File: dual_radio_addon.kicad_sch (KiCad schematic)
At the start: 36 parts, among them J1 Mainboard, J2 Antenna switcher, J3 I2C, J4 I3C, U1 Module 1, U2 74LVC1GU04, U3 24C02BN, U4 Module 2, U5 74LVC1GU04, U6 Module 3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

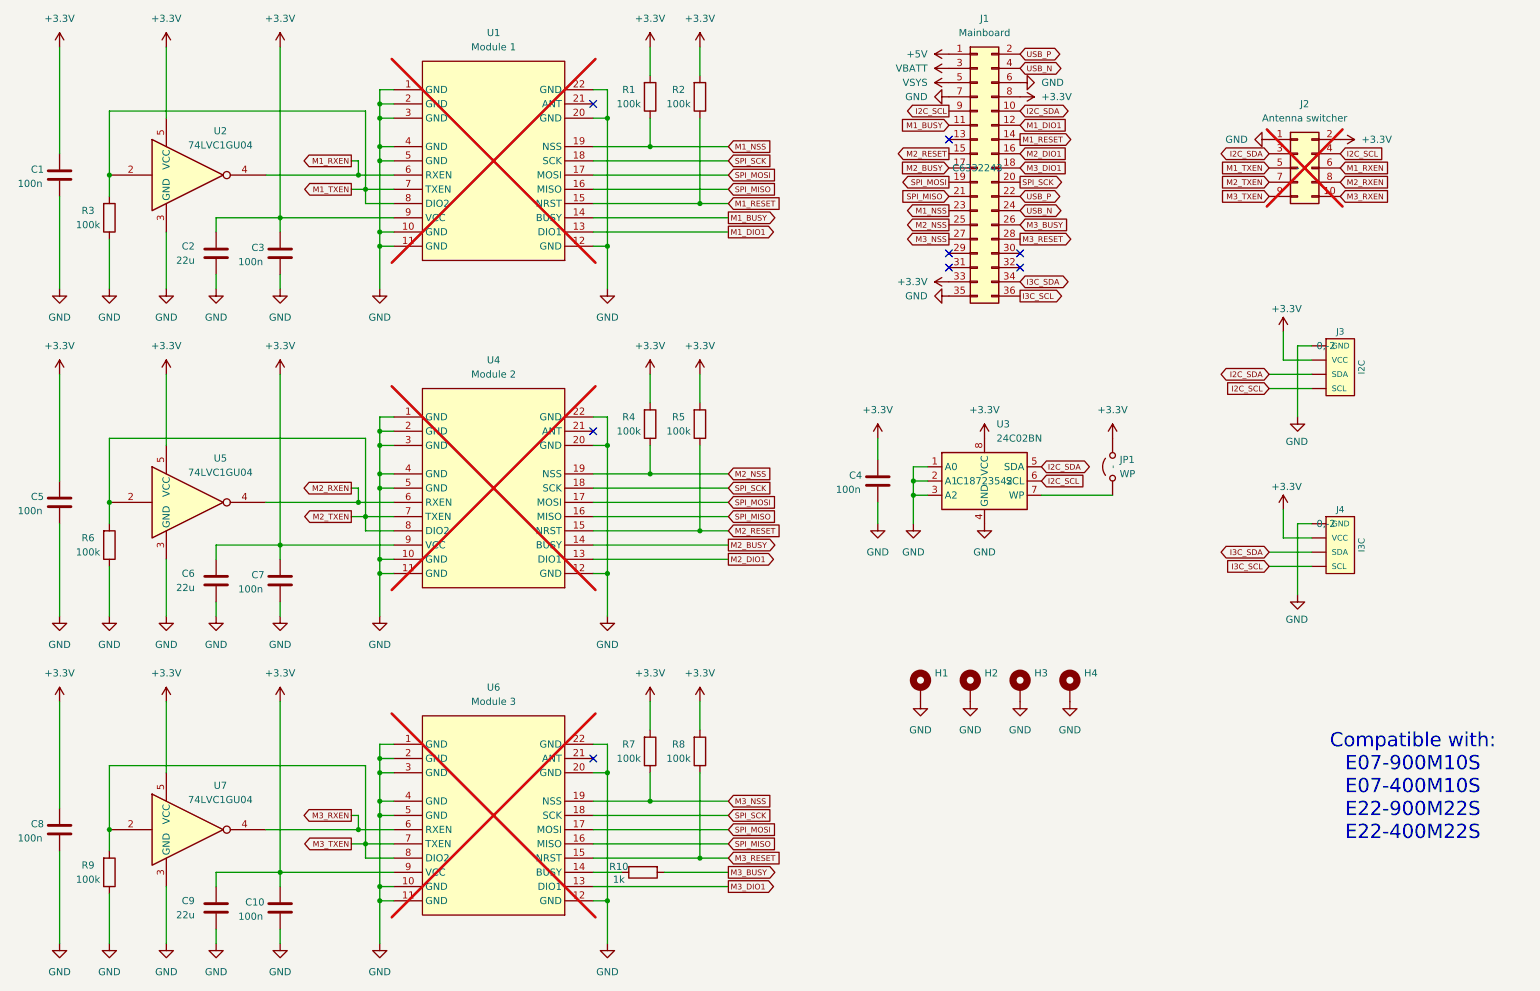
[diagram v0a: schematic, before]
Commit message: Fix connector orientation
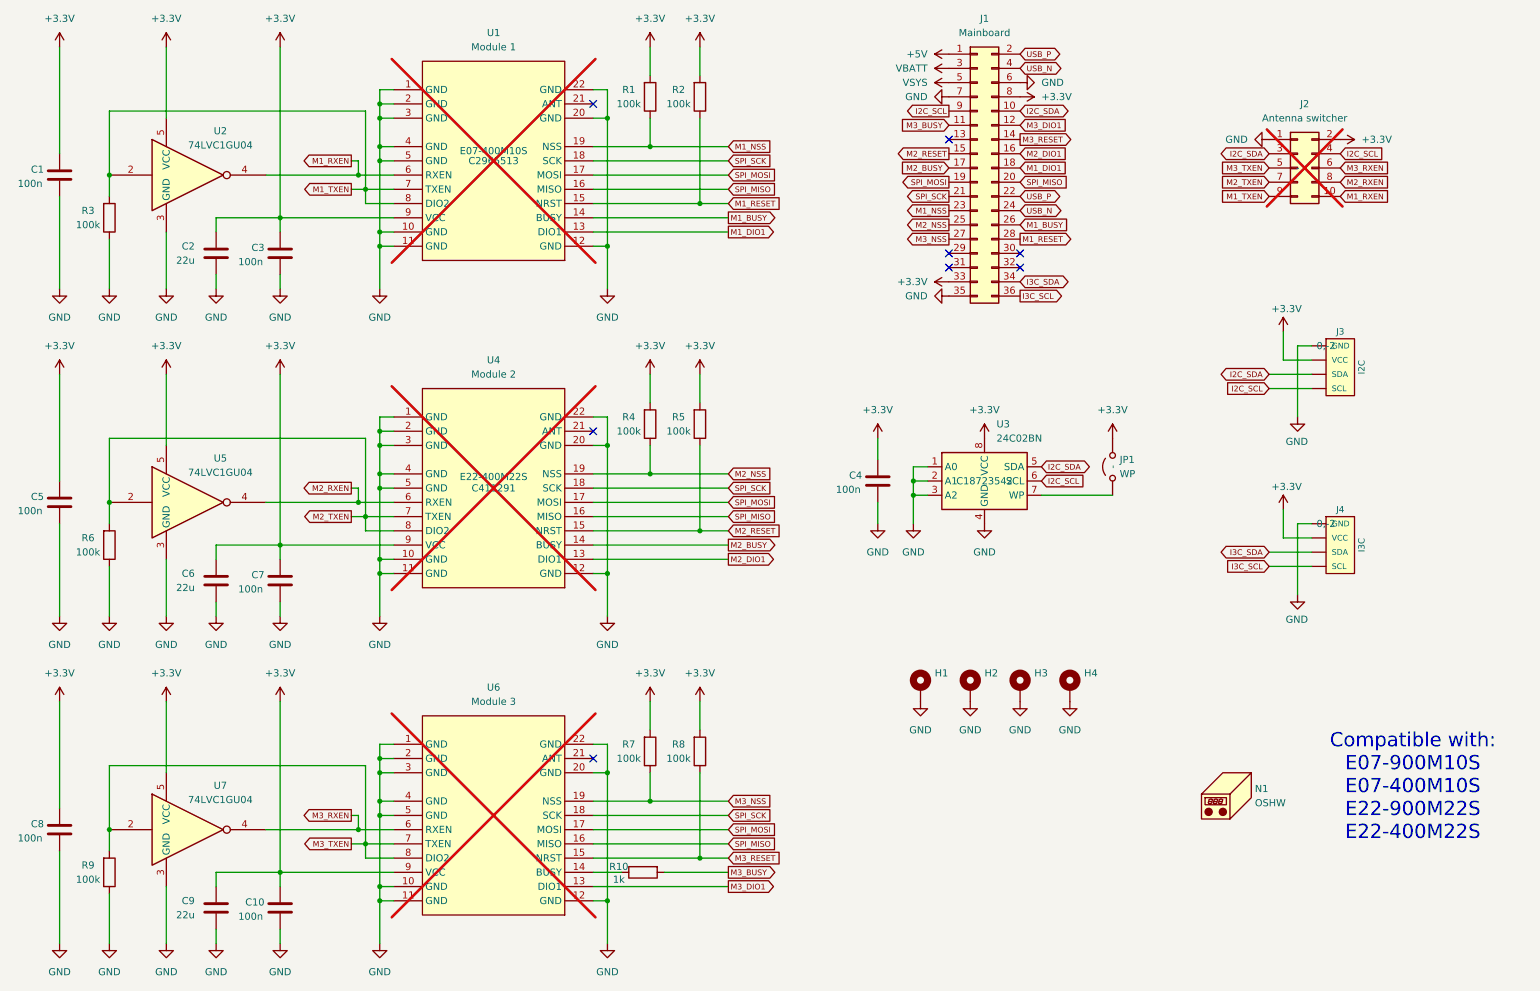
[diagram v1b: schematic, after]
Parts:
- added N1: OSHW, Symbol:OSHW-Logo2_9.8x8mm_SilkScreen, symbol Mechanical:Housing
- J2: footprint Connector_PinHeader_2.54mm:PinHeader_2x05_P2.54mm_Vertical_SMD -> Connector_PinHeader_2.54mm:PinHeader_2x05_P2.54mm_Vertical
- U1: LCSC - -> C2965513
- U4: LCSC - -> C411291
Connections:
- net M1_BUSY: now also J1.26 (Pin_26); no longer J1.11 (Pin_11)
- net M1_DIO1: now also J1.18 (Pin_18); no longer J1.12 (Pin_12)
- net M1_RESET: now also J1.28 (Pin_28); no longer J1.14 (Pin_14)
- net M1_RXEN: now also J2.10 (Pin_10); no longer J2.6 (Pin_6)
- net M1_TXEN: now also J2.9 (Pin_9); no longer J2.5 (Pin_5)
- net M3_BUSY: now also J1.11 (Pin_11); no longer J1.26 (Pin_26)
- net M3_DIO1: now also J1.12 (Pin_12); no longer J1.18 (Pin_18)
- net M3_RESET: now also J1.14 (Pin_14); no longer J1.28 (Pin_28)
- net M3_RXEN: now also J2.6 (Pin_6); no longer J2.10 (Pin_10)
- net M3_TXEN: now also J2.5 (Pin_5); no longer J2.9 (Pin_9)
- net SPI_MISO: now also J1.20 (Pin_20); no longer J1.21 (Pin_21)
- net SPI_SCK: now also J1.21 (Pin_21); no longer J1.20 (Pin_20)
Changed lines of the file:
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@@
 	(global_label "M1_DIO1"
 		(shape input)
-		(at 198.12 36.83 0)
+		(at 198.12 44.45 0)
 		(fields_autoplaced yes)
 		(effects
@@
 		)
 		(property "Intersheetrefs" "${INTERSHEET_REFS}"
-			(at 206.9425 36.83 0)
+			(at 206.9425 44.45 0)
 			(effects
 				(font
@@
 	(global_label "SPI_MISO"
 		(shape input)
-		(at 185.42 49.53 180)
+		(at 198.12 46.99 0)
 		(fields_autoplaced yes)
 		(effects
@@
 				(size 1.016 1.016)
 			)
-			(justify right)
+			(justify left)
 		)
 		(property "Intersheetrefs" "${INTERSHEET_REFS}"
-			(at 176.1137 49.53 0)
+			(at 207.4263 46.99 0)
 			(effects
 				(font
 					(size 1.27 1.27)
 				)
-				(justify right)
+				(justify left)
 				(hide yes)
 			)
@@
 	(global_label "M3_TXEN"
 		(shape input)
-		(at 242.57 49.53 180)
+		(at 242.57 44.45 180)
 		(fields_autoplaced yes)
 		(effects
@@
 		)
 		(property "Intersheetrefs" "${INTERSHEET_REFS}"
-			(at 233.554 49.53 0)
+			(at 233.554 44.45 0)
 			(effects
 				(font
@@
 	(global_label "M1_RESET"
 		(shape output)
-		(at 198.12 39.37 0)
+		(at 198.12 57.15 0)
 		(fields_autoplaced yes)
 		(effects
@@
 		)
 		(property "Intersheetrefs" "${INTERSHEET_REFS}"
-			(at 208.0068 39.37 0)
+			(at 208.0068 57.15 0)
 			(effects
 				(font
@@
 	(global_label "M1_RXEN"
 		(shape input)
-		(at 255.27 44.45 0)
+		(at 255.27 49.53 0)
 		(fields_autoplaced yes)
 		(effects
@@
 		)
 		(property "Intersheetrefs" "${INTERSHEET_REFS}"
-			(at 264.5279 44.45 0)
+			(at 264.5279 49.53 0)
 			(effects
 				(font
@@
 	(global_label "M3_DIO1"
 		(shape input)
-		(at 198.12 44.45 0)
+		(at 198.12 36.83 0)
 		(fields_autoplaced yes)
 		(effects
@@
 		)
 		(property "Intersheetrefs" "${INTERSHEET_REFS}"
-			(at 206.9425 44.45 0)
+			(at 206.9425 36.83 0)
 			(effects
 				(font
@@
 	(global_label "M3_BUSY"
 		(shape input)
-		(at 198.12 54.61 0)
+		(at 185.42 36.83 180)
 		(fields_autoplaced yes)
 		(effects
@@
 				(size 1.016 1.016)
 			)
-			(justify left)
+			(justify right)
 		)
 		(property "Intersheetrefs" "${INTERSHEET_REFS}"
-			(at 207.3296 54.61 0)
+			(at 176.2104 36.83 0)
 			(effects
 				(font
 					(size 1.27 1.27)
 				)
-				(justify left)
+				(justify right)
 				(hide yes)
 			)
@@
 	(global_label "M3_RXEN"
 		(shape input)
-		(at 255.27 49.53 0)
+		(at 255.27 44.45 0)
 		(fields_autoplaced yes)
 		(effects
@@
 		)
 		(property "Intersheetrefs" "${INTERSHEET_REFS}"
-			(at 264.5279 49.53 0)
+			(at 264.5279 44.45 0)
 			(effects
 				(font
@@
 	(global_label "M1_TXEN"
 		(shape input)
-		(at 242.57 44.45 180)
+		(at 242.57 49.53 180)
 		(fields_autoplaced yes)
 		(effects
@@
 		)
 		(property "Intersheetrefs" "${INTERSHEET_REFS}"
-			(at 233.554 44.45 0)
+			(at 233.554 49.53 0)
 			(effects
 				(font
@@
 	(global_label "SPI_SCK"
 		(shape output)
-		(at 198.12 46.99 0)
+		(at 185.42 49.53 180)
 		(fields_autoplaced yes)
 		(effects
@@
 				(size 1.016 1.016)
 			)
-			(justify left)
+			(justify right)
 		)
 		(property "Intersheetrefs" "${INTERSHEET_REFS}"
-			(at 206.749 46.99 0)
+			(at 176.791 49.53 0)
 			(effects
 				(font
 					(size 1.27 1.27)
 				)
-				(justify left)
+				(justify right)
 				(hide yes)
 			)
@@
 	(global_label "M3_RESET"
 		(shape output)
-		(at 198.12 57.15 0)
+		(at 198.12 39.37 0)
 		(fields_autoplaced yes)
 		(effects
@@
 		)
 		(property "Intersheetrefs" "${INTERSHEET_REFS}"
-			(at 208.0068 57.15 0)
+			(at 208.0068 39.37 0)
 			(effects
 				(font
@@
 	(global_label "M1_BUSY"
 		(shape input)
-		(at 185.42 36.83 180)
+		(at 198.12 54.61 0)
 		(fields_autoplaced yes)
 		(effects
@@
 				(size 1.016 1.016)
 			)
-			(justify right)
+			(justify left)
 		)
 		(property "Intersheetrefs" "${INTERSHEET_REFS}"
-			(at 176.2104 36.83 0)
+			(at 207.3296 54.61 0)
 			(effects
 				(font
 					(size 1.27 1.27)
 				)
-				(justify right)
+				(justify left)
 				(hide yes)
 			)
@@
 					(size 1.27 1.27)
 				)
+				(hide yes)
 			)
 		)
@@
 	)
 	(symbol
+		(lib_id "Mechanical:Housing")
+		(at 236.22 156.21 0)
+		(unit 1)
+		(exclude_from_sim no)
+		(in_bom no)
+		(on_board yes)
+		(dnp no)
+		(fields_autoplaced yes)
+		(property "Reference" "N1"
+			(at 240.03 155.2574 0)
+			(effects
+				(font
+					(size 1.27 1.27)
+				)
+				(justify left)
+			)
+		)
+		(property "Value" "OSHW"
+			(at 240.03 157.7974 0)
+			(effects
+				(font
+					(size 1.27 1.27)
+				)
+				(justify left)
+			)
+		)
+		(property "Footprint" "Symbol:OSHW-Logo2_9.8x8mm_SilkScreen"
+			(at 237.49 154.94 0)
+			(effects
+				(font
+					(size 1.27 1.27)
+				)
+				(hide yes)
+			)
+		)
+		(property "Datasheet" "~"
+			(at 237.49 154.94 0)
+			(effects
+				(font
+					(size 1.27 1.27)
+				)
+				(hide yes)
+			)
+		)
+		(property "Description" "Housing"
+			(at 236.22 156.21 0)
+			(effects
+				(font
+					(size 1.27 1.27)
+				)
+				(hide yes)
+			)
+		)
+		(instances
+			(project ""
+				(path "/2205494a-02fa-46fe-bb1d-f2ff6c95af95"
+					(reference "N1")
+					(unit 1)
+				)
+			)
+		)
+	)
+	(symbol
 		(lib_id "power:+5V")
 		(at 185.42 26.67 90)
@@
 		(on_board yes)
 		(dnp yes)
-		(fields_autoplaced yes)
 		(property "Reference" "U1"
 			(at 104.14 20.32 0)
@@
 			)
 		)
-		(property "Description" ""
-			(at 104.14 43.18 0)
+		(property "Description" "E07-400M10S"
+			(at 104.14 41.402 0)
 			(effects
 				(font
 					(size 1.27 1.27)
 				)
-				(hide yes)
 			)
 		)
-		(property "LCSC" "-"
+		(property "LCSC" "C2965513"
 			(at 104.14 43.18 0)
 			(effects
@@
 		(on_board yes)
 		(dnp yes)
-		(fields_autoplaced yes)
 		(property "Reference" "U4"
 			(at 104.14 78.74 0)
@@
 			)
 		)
-		(property "Description" ""
-			(at 104.14 101.6 0)
+		(property "Description" "E22-400M22S"
+			(at 104.14 99.568 0)
 			(effects
 				(font
 					(size 1.27 1.27)
 				)
-				(hide yes)
 			)
 		)
-		(property "LCSC" "-"
+		(property "LCSC" "C411291"
 			(at 104.14 101.6 0)
 			(effects
@@
 			)
 		)
-		(property "Footprint" "Connector_PinHeader_2.54mm:PinHeader_2x05_P2.54mm_Vertical_SMD"
+		(property "Footprint" "Connector_PinHeader_2.54mm:PinHeader_2x05_P2.54mm_Vertical"
 			(at 247.65 44.45 0)
 			(effects

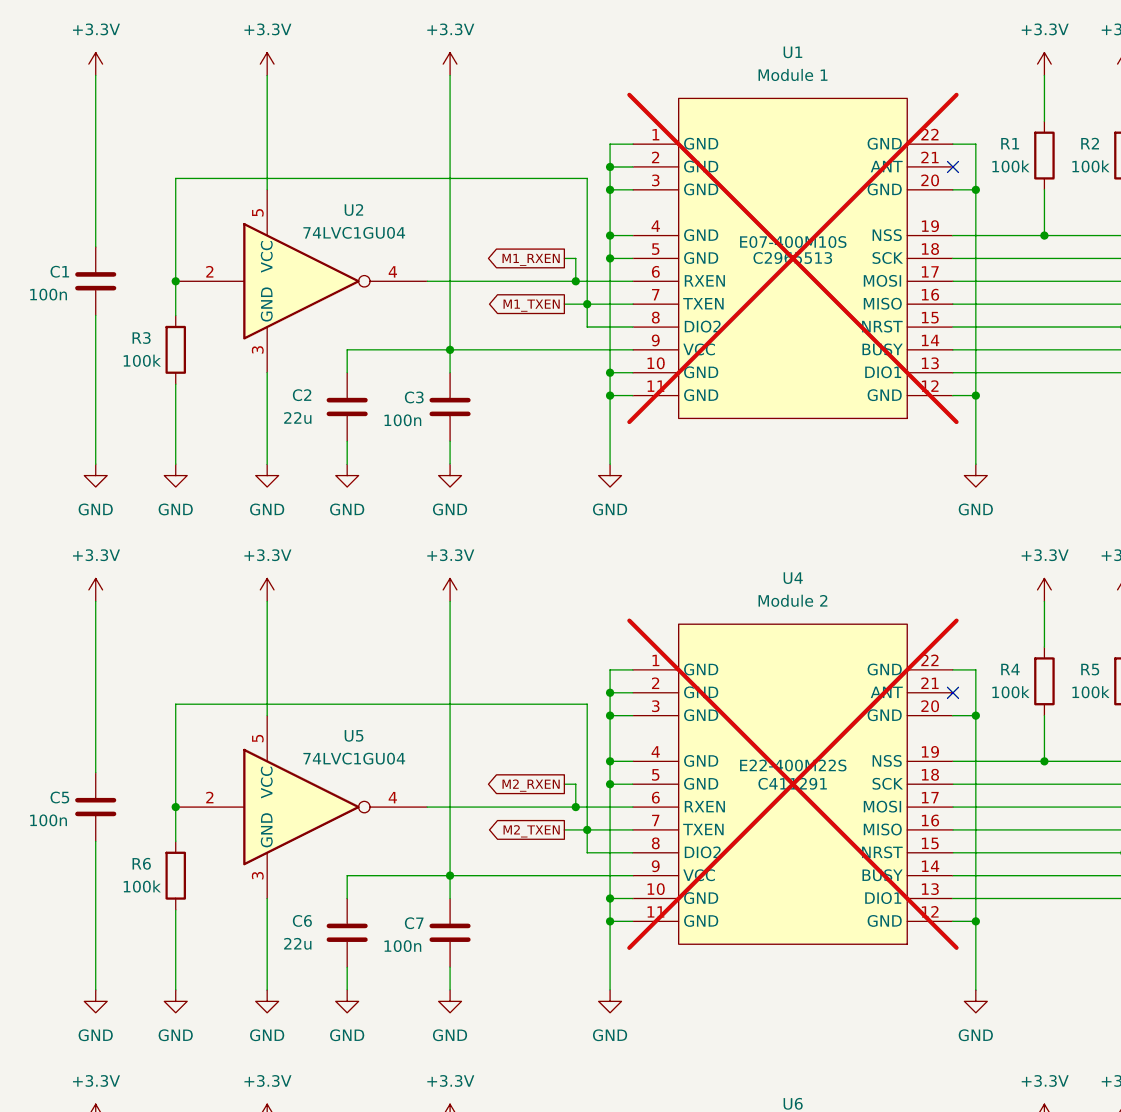
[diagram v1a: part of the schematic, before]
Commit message: Configure first two radio modules to be populated by manufacturer
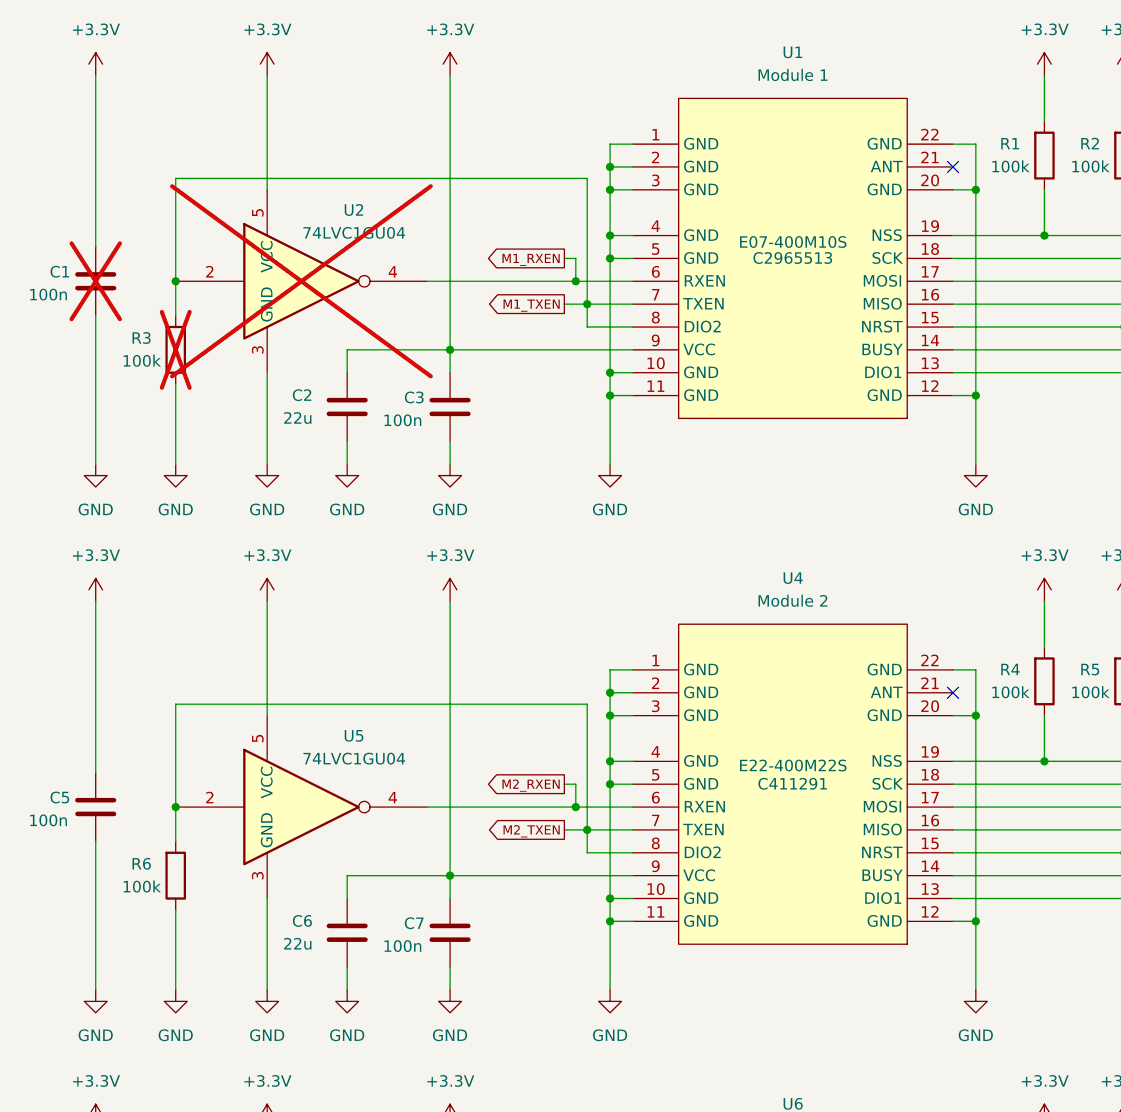
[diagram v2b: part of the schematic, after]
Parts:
- C1, R3, U2: now not fitted; now left out of the parts list
- U1, U4: now fitted
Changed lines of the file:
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@@
 		(in_bom yes)
 		(on_board yes)
-		(dnp yes)
+		(dnp no)
 		(property "Reference" "U1"
 			(at 104.14 20.32 0)
@@
 		(unit 1)
 		(exclude_from_sim no)
-		(in_bom yes)
+		(in_bom no)
 		(on_board yes)
-		(dnp no)
+		(dnp yes)
 		(property "Reference" "C1"
 			(at 23.876 44.704 0)
@@
 		(unit 1)
 		(exclude_from_sim no)
-		(in_bom yes)
+		(in_bom no)
 		(on_board yes)
-		(dnp no)
+		(dnp yes)
 		(property "Reference" "R3"
 			(at 31.75 52.07 0)
@@
 		(in_bom yes)
 		(on_board yes)
-		(dnp yes)
+		(dnp no)
 		(property "Reference" "U4"
 			(at 104.14 78.74 0)
@@
 		(unit 1)
 		(exclude_from_sim no)
-		(in_bom yes)
+		(in_bom no)
 		(on_board yes)
-		(dnp no)
+		(dnp yes)
 		(property "Reference" "U2"
 			(at 55.372 37.846 0)
